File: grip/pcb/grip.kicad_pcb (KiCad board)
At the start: 2 copper layers, 4 parts, among them U1 MAN71A, U2 MAN71A

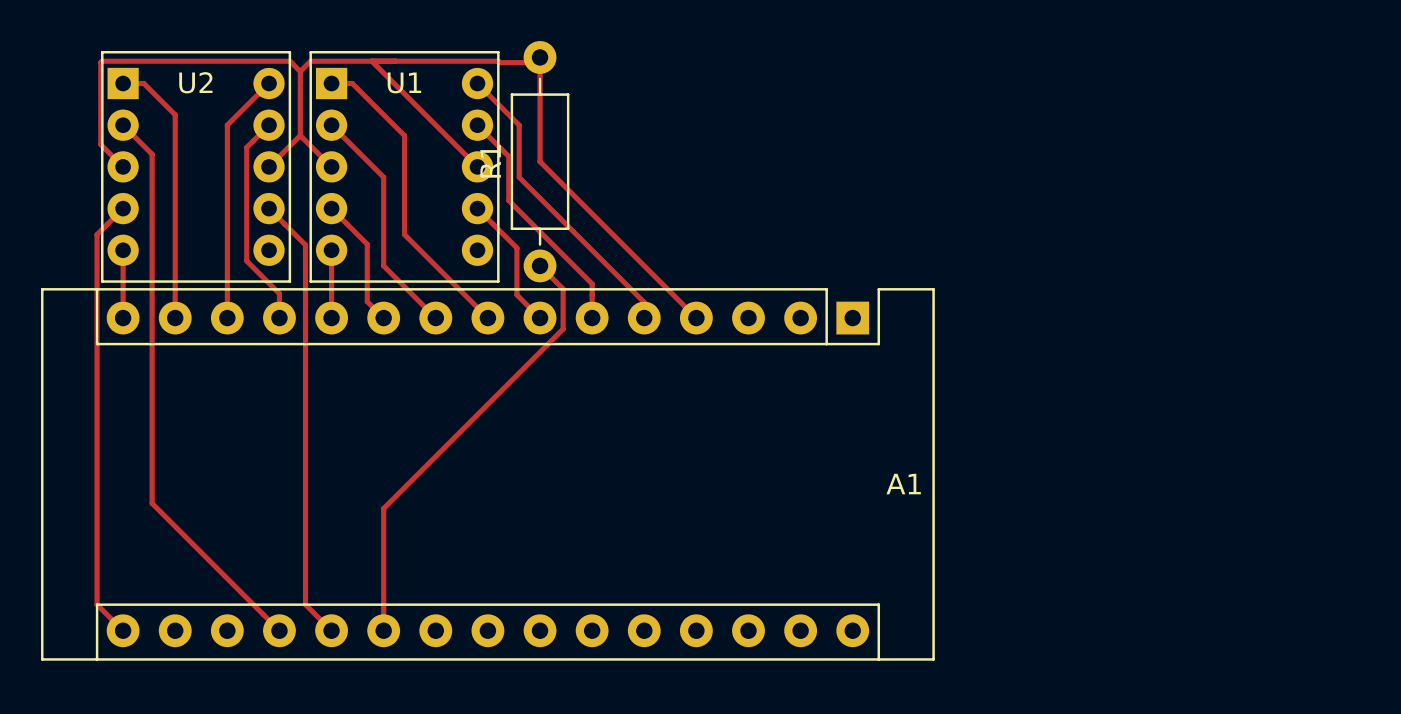
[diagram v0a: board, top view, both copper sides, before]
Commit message: grip: changed pcb for a line layout
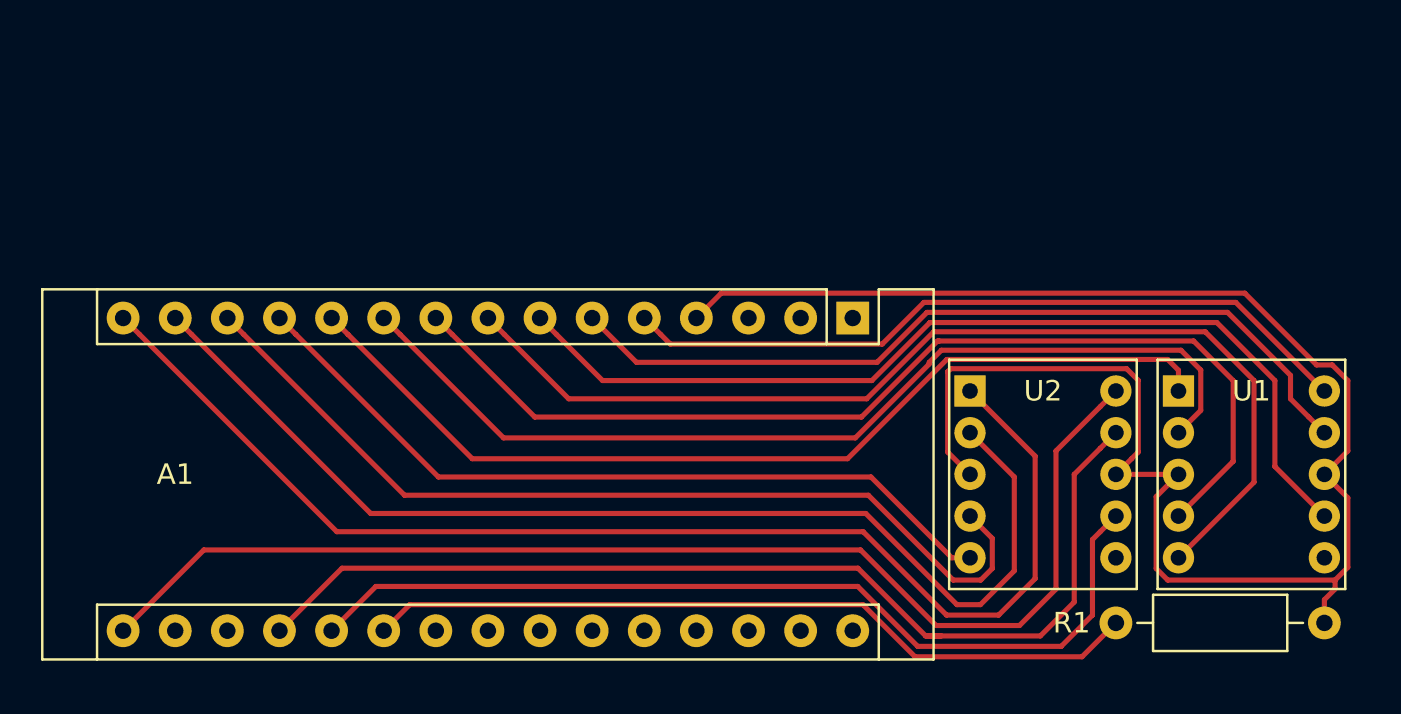
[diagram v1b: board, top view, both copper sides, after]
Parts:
- moved U1 43.9 mm to (160.7, 98.8)
- moved U2 43.9 mm to (150.5, 98.8)
- moved R1 33.0 mm to (157.6, 110.1), turned to 0 degrees
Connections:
- A1 pad 10: unit_E -> unit_F
- A1 pad 11: unit_D -> unit_G
- A1 pad 12: deci_B -> deci_D
- A1 pad 13: deci_A -> deci_E
- A1 pad 14: deci_G -> deci_F
- A1 pad 15: deci_D -> deci_G
- A1 pad 16: deci_E -> deci_A
- A1 pad 19: deci_F -> deci_B
- A1 pad 8: unit_G -> unit_D
- A1 pad 9: unit_F -> unit_E
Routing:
- net deci_G: track 13.1 -> 61.6 mm
- net unit_D: track 3.30 -> 51.5 mm
- net deci_A: track 12.3 -> 60.2 mm
- net unit_E: track 6.39 -> 50.9 mm
- net deci_B: track 10.5 -> 51.9 mm
- net unit_C: track 6.60 -> 47.0 mm
- net unit_F: track 11.5 -> 48.0 mm
- net deci_D: track 3.30 -> 38.5 mm
- net unit_G: track 15.2 -> 47.3 mm
- net unit_B: track 11.7 -> 40.7 mm
- net deci_F: track 27.8 -> 55.0 mm
- net GND: track 59.3 -> 84.4 mm
- net deci_E: track 21.6 -> 45.8 mm
- net deci_C: track 21.8 -> 45.1 mm
- net unit_A: track 14.8 -> 36.3 mm
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
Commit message: added gnd plane
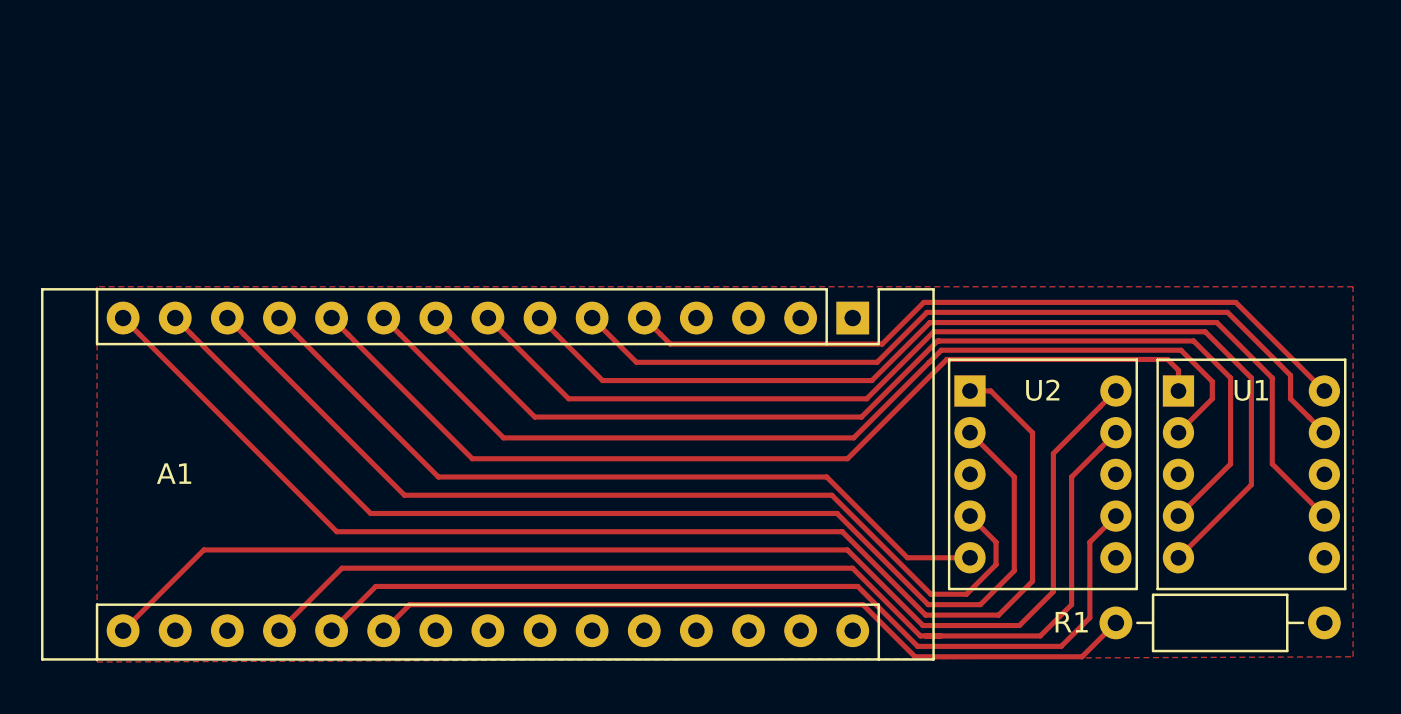
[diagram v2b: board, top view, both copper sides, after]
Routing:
- net GND: track 84.4 -> 0.00 mm
- net deci_E: track 45.8 -> 46.5 mm
- added copper zone on F.Cu, net GND

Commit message: correcte mutt template
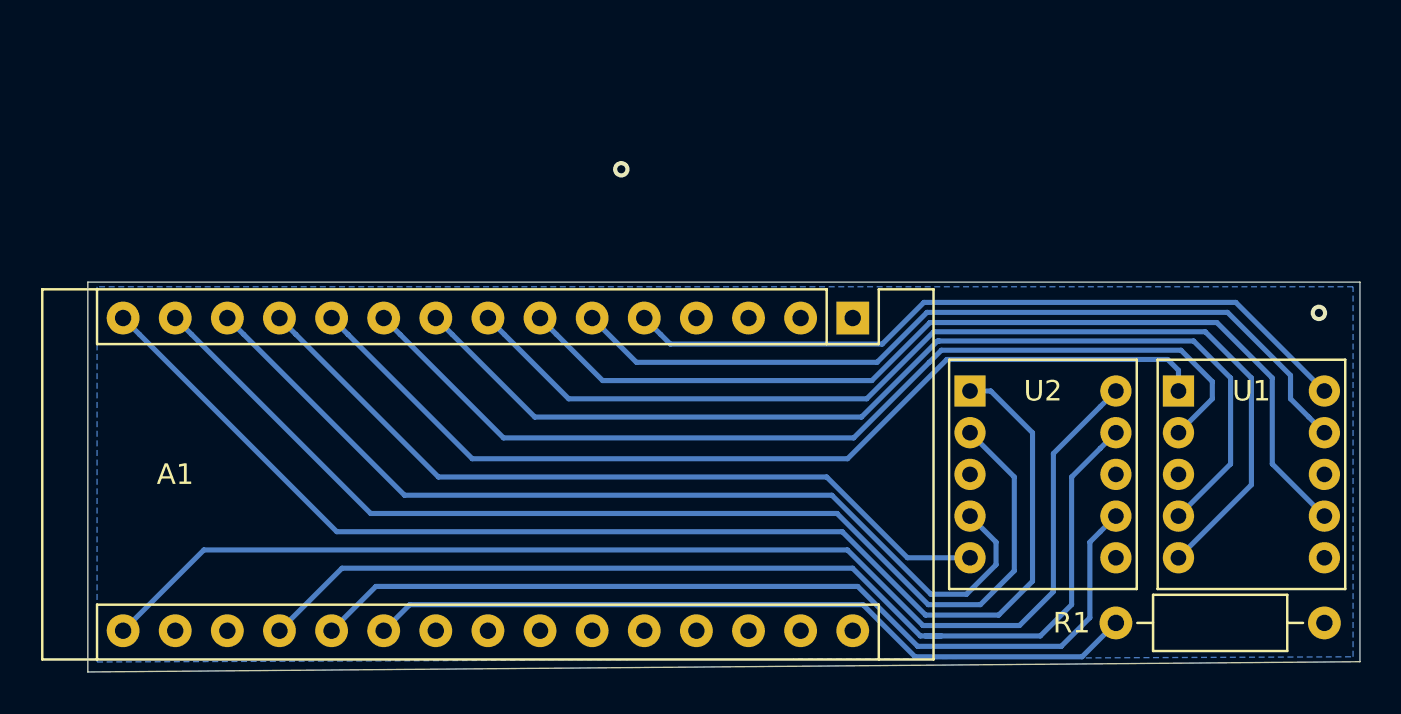
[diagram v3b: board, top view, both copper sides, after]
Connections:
- A1 pad 29: Net-(A1-Pad29) -> GND
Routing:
- net GND: vias 0 -> 1
- net (no net): vias 0 -> 1
- added copper zone on B.Cu, net GND
- removed copper zone on F.Cu, net GND
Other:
- board outline added: 62 x 19 mm
